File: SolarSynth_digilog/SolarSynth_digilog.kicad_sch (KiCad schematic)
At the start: 31 parts, among them J1 OutputJack1, J2 Conn_01x01_Pin, J3 Conn_01x01_Pin, P1 PiezoDisc, P2 PiezoDisc, U1 74HC14, U2 MCP6002-xMC

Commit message: fixed some bugs
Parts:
- J1: footprint 007_dusjagr:AUDIO-JACK-3.5mm_SMD_noHole -> 002_Solarpunk:AUDIO-JACK-3.5mm_SMD_noHole
- J2, J3: footprint 007_dusjagr:SolarPad_VCC -> 002_Solarpunk:SolarPad_VCC
- Pad1, Pad2, Pad3, Pad4, Pad5, Pad6: footprint 007_dusjagr:SolderPad_small -> 002_Solarpunk:SolderPad_small
- U1: footprint 007_dusjagr:DIP-14_W7.62mm_LongerPads -> 002_Solarpunk:DIP-14_W7.62mm_LongerPads
- U2: footprint 007_dusjagr:DIP-8_W7.62mm_LongerPads -> Package_DIP:DIP-8_W7.62mm_LongPads
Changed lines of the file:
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@@
 			)
 		)
-		(property "Footprint" "007_dusjagr:AUDIO-JACK-3.5mm_SMD_noHole"
+		(property "Footprint" "002_Solarpunk:AUDIO-JACK-3.5mm_SMD_noHole"
 			(at 181.61 149.86 0)
 			(effects
@@
 			)
 		)
-		(property "Footprint" "007_dusjagr:DIP-8_W7.62mm_LongerPads"
+		(property "Footprint" "Package_DIP:DIP-8_W7.62mm_LongPads"
 			(at 100.33 175.26 0)
 			(effects
@@
 			)
 		)
-		(property "Footprint" "007_dusjagr:DIP-8_W7.62mm_LongerPads"
+		(property "Footprint" "Package_DIP:DIP-8_W7.62mm_LongPads"
 			(at 142.24 139.7 0)
 			(effects
@@
 			)
 		)
-		(property "Footprint" "007_dusjagr:SolderPad_small"
+		(property "Footprint" "002_Solarpunk:SolderPad_small"
 			(at 185.42 62.23 0)
 			(effects
@@
 			)
 		)
-		(property "Footprint" "007_dusjagr:SolderPad_small"
+		(property "Footprint" "002_Solarpunk:SolderPad_small"
 			(at 105.41 64.77 0)
 			(effects
@@
 			)
 		)
-		(property "Footprint" "007_dusjagr:SolderPad_small"
+		(property "Footprint" "002_Solarpunk:SolderPad_small"
 			(at 200.66 105.41 0)
 			(effects
@@
 			)
 		)
-		(property "Footprint" "007_dusjagr:DIP-14_W7.62mm_LongerPads"
+		(property "Footprint" "002_Solarpunk:DIP-14_W7.62mm_LongerPads"
 			(at 83.82 100.33 0)
 			(effects
@@
 			)
 		)
-		(property "Footprint" "007_dusjagr:DIP-14_W7.62mm_LongerPads"
+		(property "Footprint" "002_Solarpunk:DIP-14_W7.62mm_LongerPads"
 			(at 224.79 100.33 0)
 			(effects
@@
 			)
 		)
-		(property "Footprint" "007_dusjagr:DIP-14_W7.62mm_LongerPads"
+		(property "Footprint" "002_Solarpunk:DIP-14_W7.62mm_LongerPads"
 			(at 52.07 100.33 0)
 			(effects
@@
 			)
 		)
-		(property "Footprint" "007_dusjagr:DIP-8_W7.62mm_LongerPads"
+		(property "Footprint" "Package_DIP:DIP-8_W7.62mm_LongPads"
 			(at 142.24 162.56 0)
 			(effects
@@
 			)
 		)
-		(property "Footprint" "007_dusjagr:DIP-14_W7.62mm_LongerPads"
+		(property "Footprint" "002_Solarpunk:DIP-14_W7.62mm_LongerPads"
 			(at 151.13 100.33 0)
 			(effects
@@
 			)
 		)
-		(property "Footprint" "007_dusjagr:SolarPad_VCC"
+		(property "Footprint" "002_Solarpunk:SolarPad_VCC"
 			(at 31.75 35.56 0)
 			(effects
@@
 			)
 		)
-		(property "Footprint" "007_dusjagr:SolderPad_small"
+		(property "Footprint" "002_Solarpunk:SolderPad_small"
 			(at 195.58 105.41 0)
 			(effects
@@
 			)
 		)
-		(property "Footprint" "007_dusjagr:DIP-14_W7.62mm_LongerPads"
+		(property "Footprint" "002_Solarpunk:DIP-14_W7.62mm_LongerPads"
 			(at 185.42 100.33 0)
 			(effects
@@
 			)
 		)
-		(property "Footprint" "007_dusjagr:DIP-14_W7.62mm_LongerPads"
+		(property "Footprint" "002_Solarpunk:DIP-14_W7.62mm_LongerPads"
 			(at 41.91 161.29 0)
 			(effects
@@
 			)
 		)
-		(property "Footprint" "007_dusjagr:SolderPad_small"
+		(property "Footprint" "002_Solarpunk:SolderPad_small"
 			(at 76.2 63.5 0)
 			(effects
@@
 			)
 		)
-		(property "Footprint" "007_dusjagr:SolarPad_VCC"
+		(property "Footprint" "002_Solarpunk:SolarPad_VCC"
 			(at 31.75 58.42 0)
 			(effects
@@
 			)
 		)
-		(property "Footprint" "007_dusjagr:DIP-14_W7.62mm_LongerPads"
+		(property "Footprint" "002_Solarpunk:DIP-14_W7.62mm_LongerPads"
 			(at 118.11 100.33 0)
 			(effects
@@
 			)
 		)
-		(property "Footprint" "007_dusjagr:SolderPad_small"
+		(property "Footprint" "002_Solarpunk:SolderPad_small"
 			(at 163.83 66.04 0)
 			(effects

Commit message: added original digilog again and moved THT-Version to a new folder
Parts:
- C1, C2, C3: footprint Capacitor_THT:C_Disc_D5.0mm_W2.5mm_P5.00mm -> 007_dusjagr:C_1210_noGND
- C4, C5: footprint Capacitor_THT:CP_Radial_D5.0mm_P2.50mm -> 007_dusjagr:C_1210_noGND
- C6, C7: footprint Capacitor_THT:C_Disc_D5.0mm_W2.5mm_P2.50mm -> 007_dusjagr:C_1210_noGND
- J1: footprint 002_Solarpunk:AUDIO-JACK-3.5mm_SMD_noHole -> 007_dusjagr:AUDIO-JACK-3.5mm_SMD_noHole
- J2, J3: footprint 002_Solarpunk:SolarPad_VCC -> 007_dusjagr:SolarPad_VCC
- Pad1, Pad2, Pad3, Pad4, Pad5, Pad6: footprint 002_Solarpunk:SolderPad_small -> 007_dusjagr:SolderPad_small
- R1, R2, R3, R4, R5, R6, R7: footprint Resistor_THT:R_Axial_DIN0309_L9.0mm_D3.2mm_P12.70mm_Horizontal -> 007_dusjagr:R_1206_noGND
- RV1, RV2: footprint blinkyparts:Potentiometer_Alpha_RD901F-40-00D_Single_Vertical_bigger-holes -> 007_dusjagr:RD901F-ALPHA-3D_minis
- RV3: footprint blinkyparts:Potentiometer_Alpha_RD901F-40-00D_Single_Vertical_bigger-holes -> 007_dusjagr:RD901F-ALPHA-3D_longpads
- U1: footprint 002_Solarpunk:DIP-14_W7.62mm_LongerPads -> 007_dusjagr:DIP-14_W7.62mm_LongerPads
- U2: footprint Package_DIP:DIP-8_W7.62mm_LongPads -> 007_dusjagr:DIP-8_W7.62mm_LongerPads
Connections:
- net VCC: now also RV3.3; no longer RV3.1
- net at C1.2, U1.3: now also RV1.3; no longer RV1.1
- net at C3.2, U1.5: now also RV2.1; no longer RV2.3
- net at R7.1: now also RV3.1; no longer RV3.3
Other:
- moved on the sheet: RV1, RV2, RV3

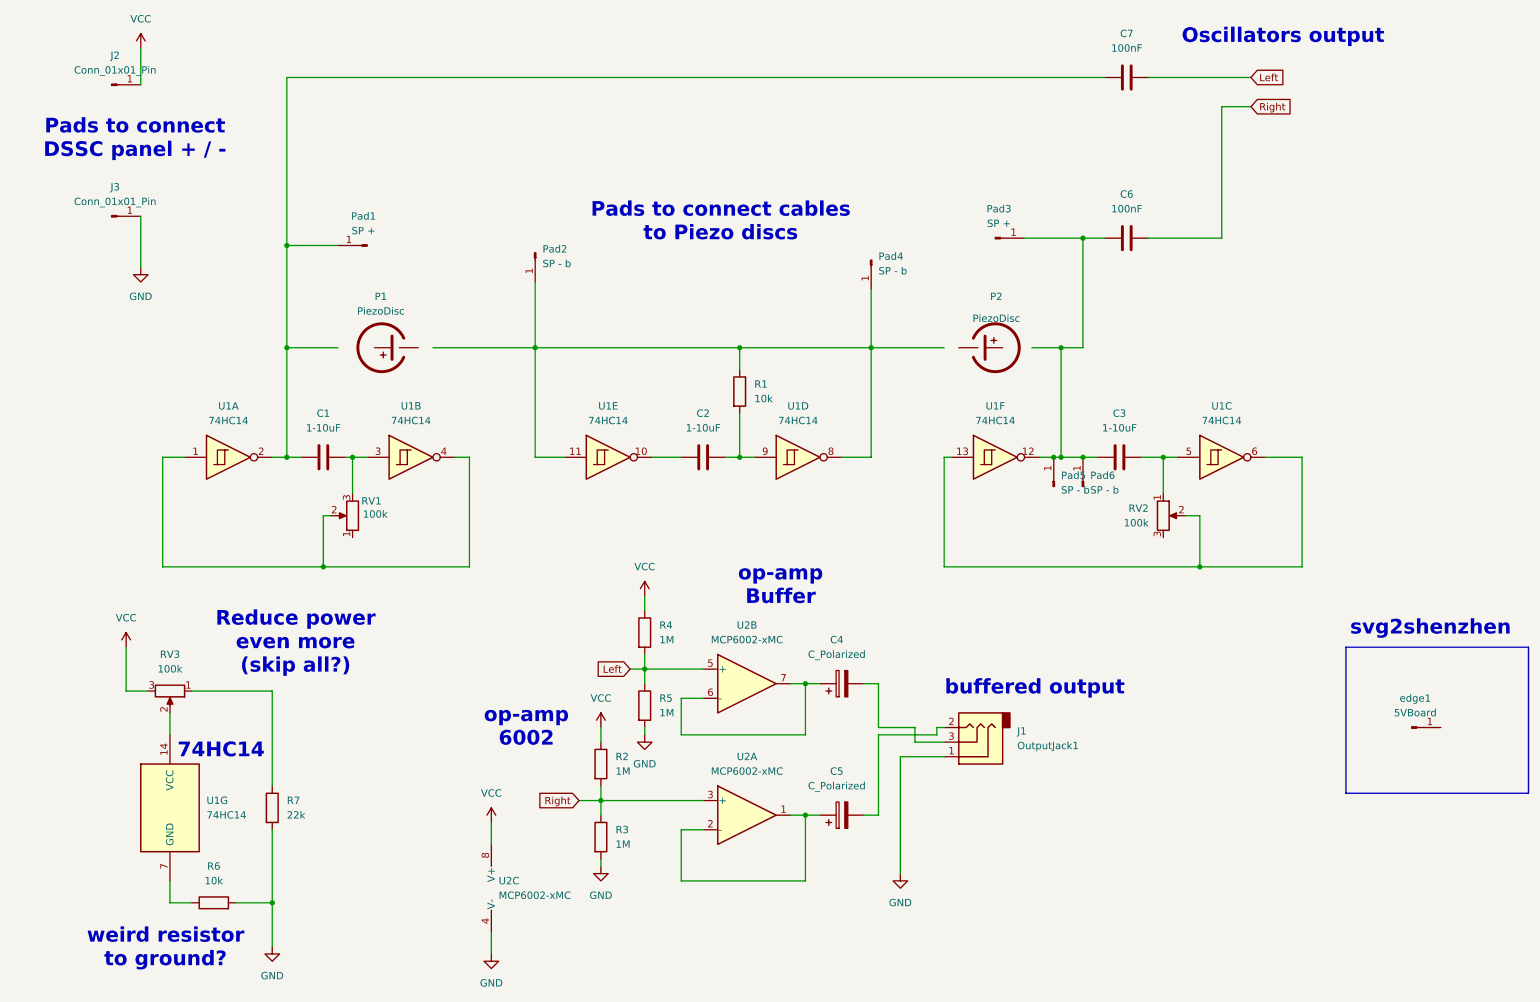
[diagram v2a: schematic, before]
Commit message: Change SMD to THT
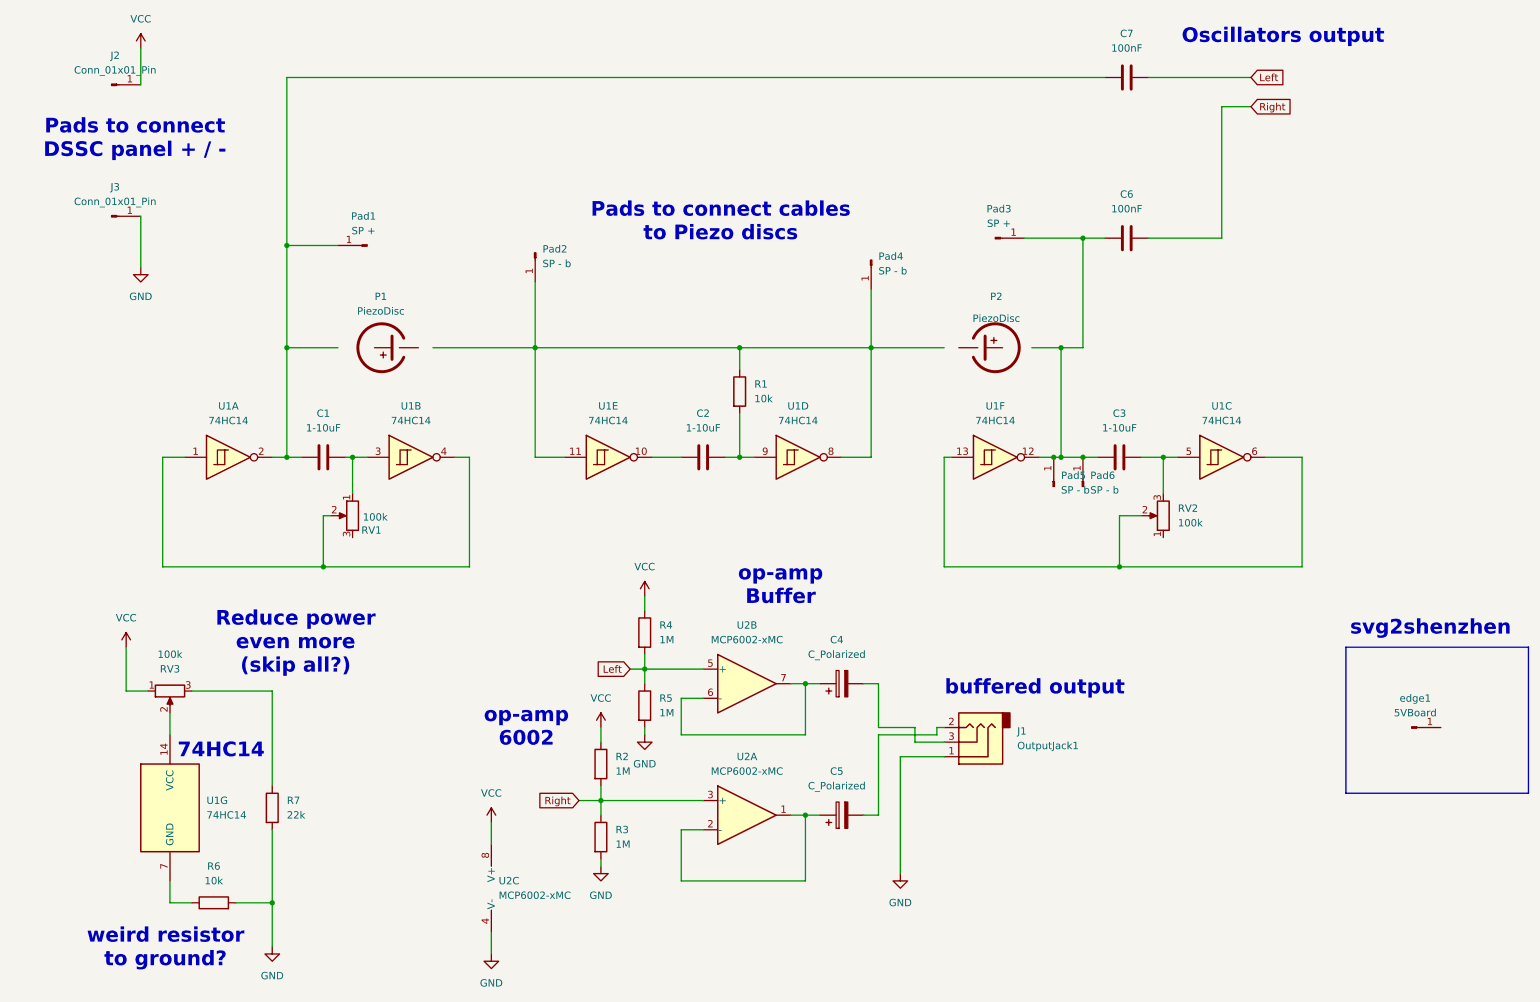
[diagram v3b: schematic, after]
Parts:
- C1, C2, C3: footprint 007_dusjagr:C_1210_noGND -> Capacitor_THT:C_Disc_D5.0mm_W2.5mm_P5.00mm
- C4, C5: footprint 007_dusjagr:C_1210_noGND -> Capacitor_THT:CP_Radial_D5.0mm_P2.50mm
- C6, C7: footprint 007_dusjagr:C_1210_noGND -> Capacitor_THT:C_Disc_D5.0mm_W2.5mm_P2.50mm
- R1, R2, R3, R4, R5, R6, R7: footprint 007_dusjagr:R_1206_noGND -> Resistor_THT:R_Axial_DIN0309_L9.0mm_D3.2mm_P12.70mm_Horizontal
- RV1, RV2: footprint 007_dusjagr:RD901F-ALPHA-3D_minis -> blinkyparts:Potentiometer_Alpha_RD901F-40-00D_Single_Vertical_bigger-holes
- RV3: footprint 007_dusjagr:RD901F-ALPHA-3D_longpads -> blinkyparts:Potentiometer_Alpha_RD901F-40-00D_Single_Vertical_bigger-holes
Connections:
- net VCC: now also RV3.1; no longer RV3.3
- net at RV1.1: now also C1.2, U1.3
- net at C3.2, U1.5: now also RV2.3; no longer RV2.1
- net at R7.1: now also RV3.3; no longer RV3.1
- now unconnected: RV1.3
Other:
- moved on the sheet: RV1, RV2, RV3
